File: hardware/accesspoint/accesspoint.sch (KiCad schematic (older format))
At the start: 14 parts

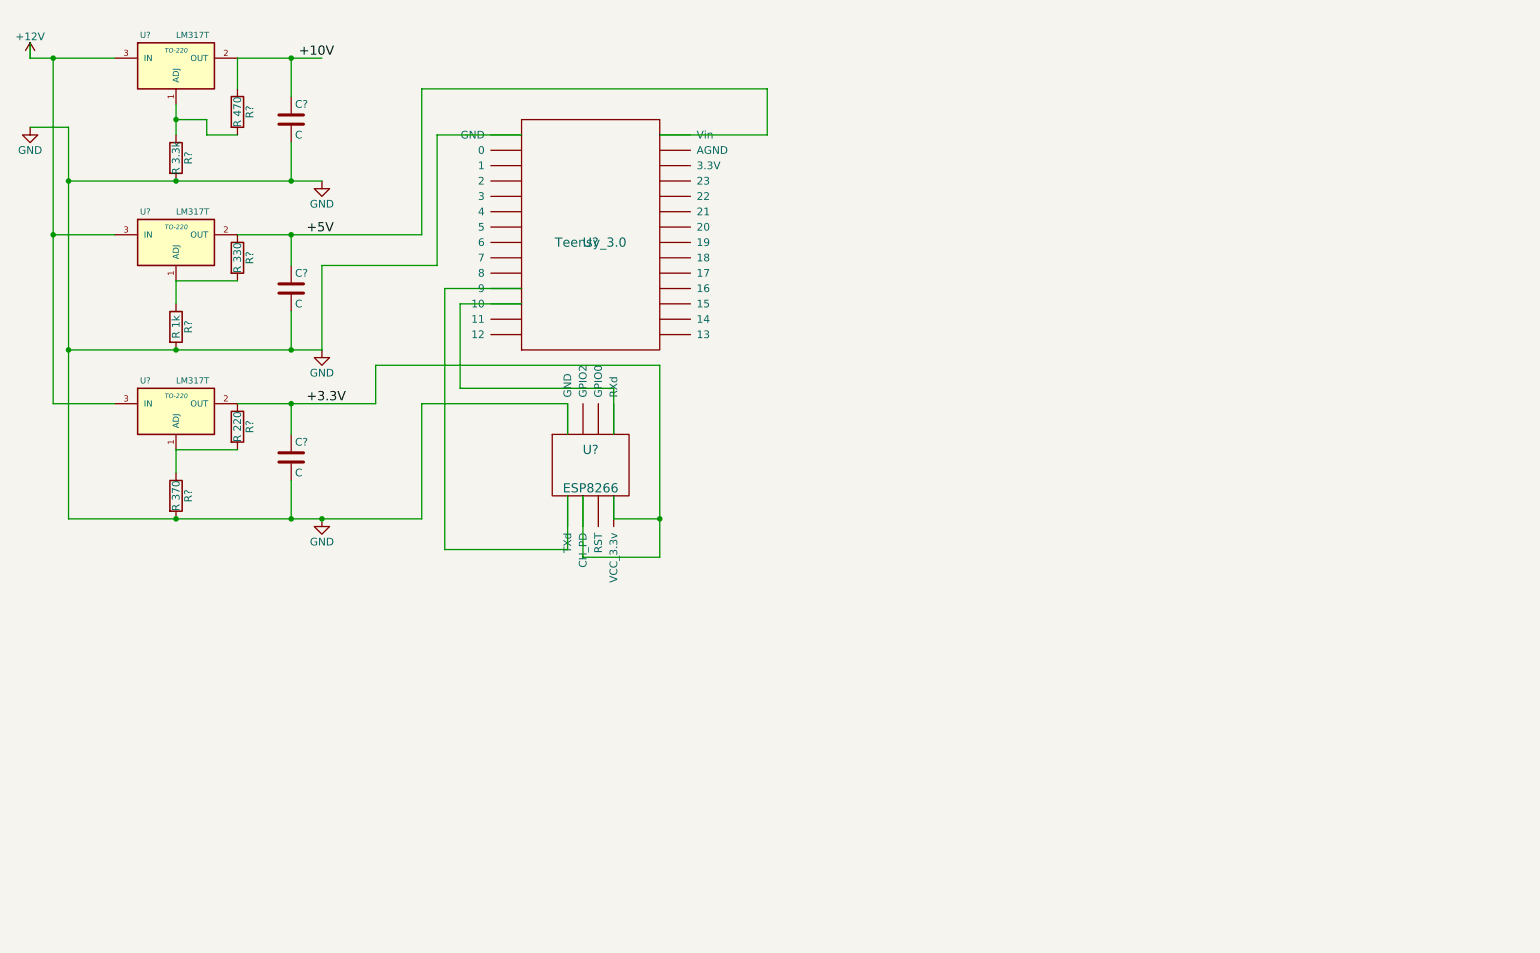
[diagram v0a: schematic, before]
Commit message: finished basic hardware design
left one spare pin available on Eth2
left one completeled unused pin on Eth1
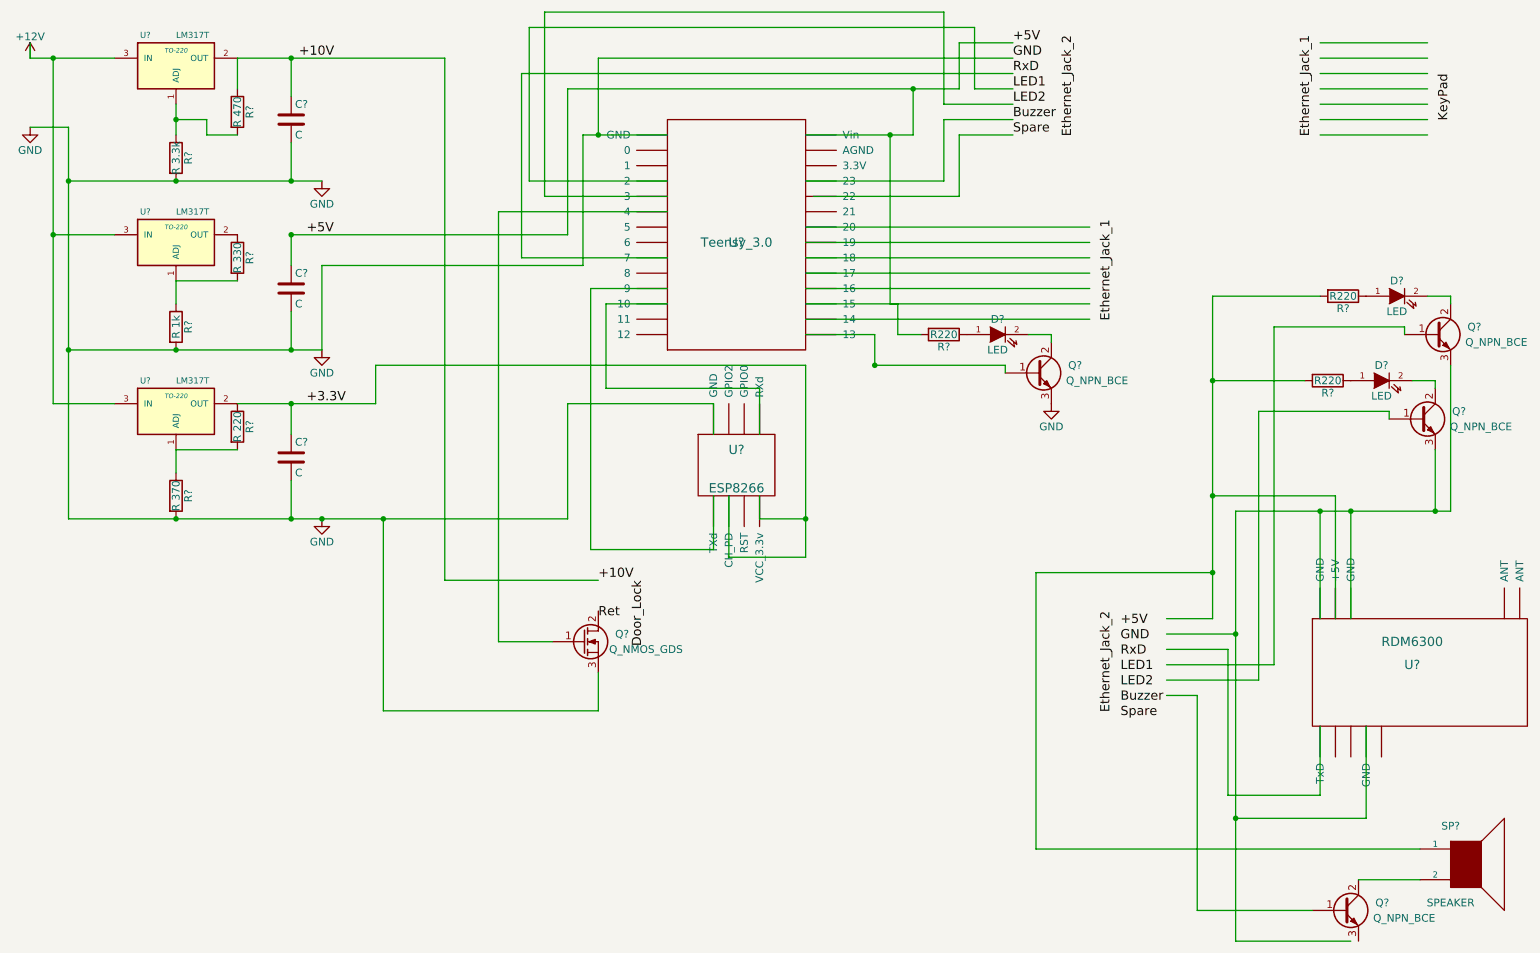
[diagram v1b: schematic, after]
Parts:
- added D? (x3): LED, symbol LED
- added Q? (x4): Q_NPN_BCE, symbol Q_NPN_BCE
- added Q?: Q_NMOS_GDS, symbol Q_NMOS_GDS
- added R? (x3): R220, symbol R
- added SP?: SPEAKER, symbol SPEAKER
- added U?: RDM6300, symbol RDM6300
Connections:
- net labels added: Buzzer, Door_Lock, Ethernet_Jack_1, Ethernet_Jack_2, KeyPad, LED1, LED2, Ret, RxD, Spare
- wire segments 54 -> 148
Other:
- moved on the sheet: U?
